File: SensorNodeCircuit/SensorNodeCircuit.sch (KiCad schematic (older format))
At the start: 12 parts

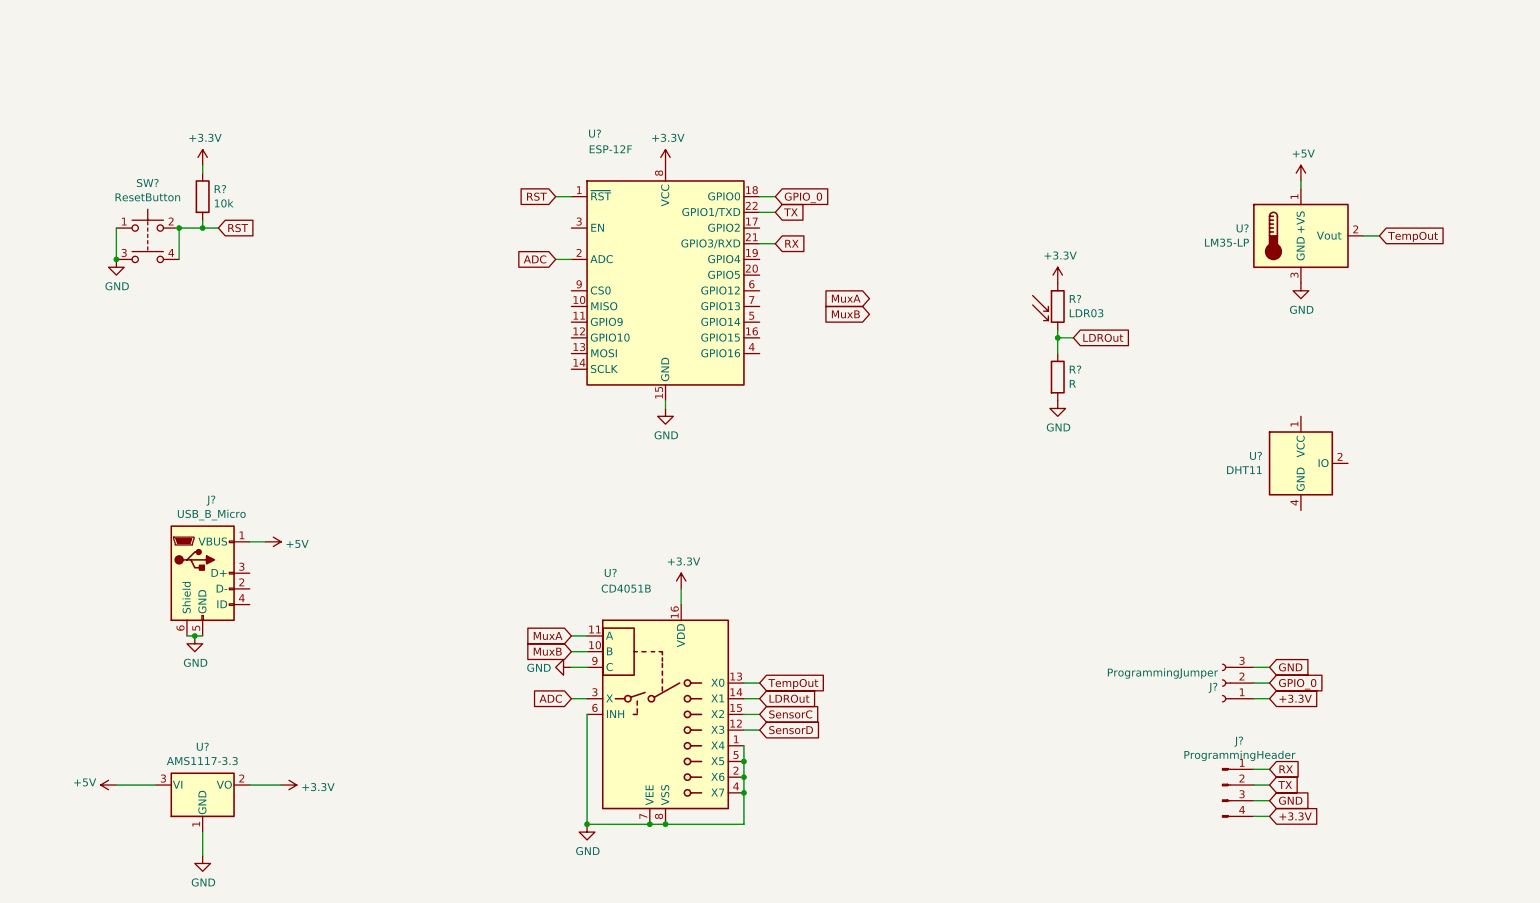
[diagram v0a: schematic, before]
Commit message: Sensor Node schematic finished
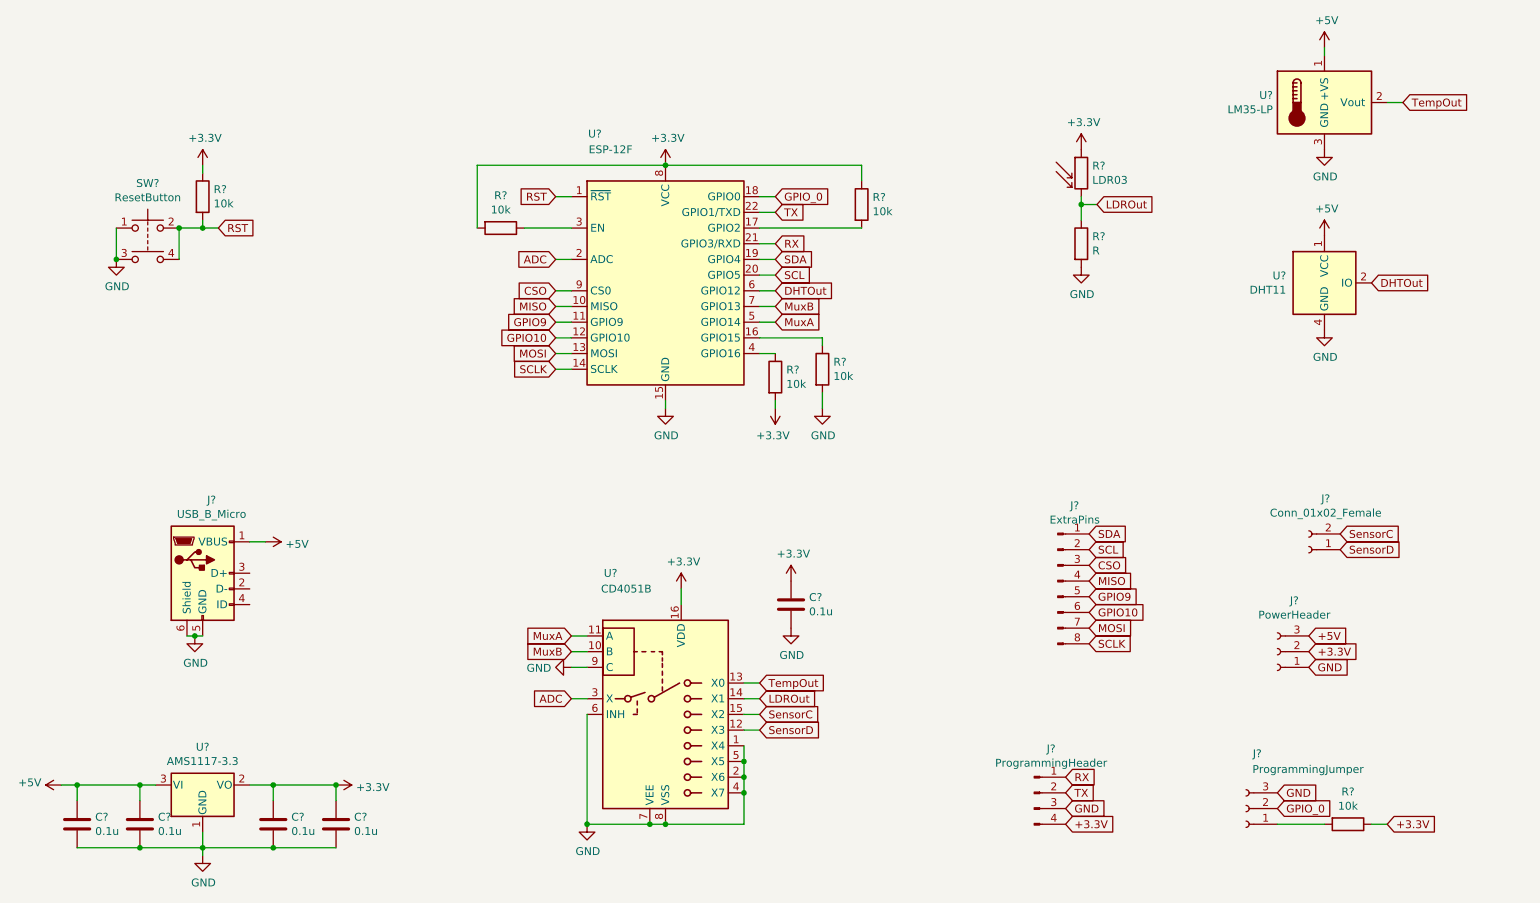
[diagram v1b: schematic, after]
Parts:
- added C? (x5): 0.1u, Capacitor_SMD:C_1206_3216Metric_Pad1.42x1.75mm_HandSolder, symbol Device:C
- added J?: ExtraPins, Connector_PinSocket_2.54mm:PinSocket_1x08_P2.54mm_Vertical, symbol Connector:Conn_01x08_Male
- added J?: PowerHeader, Connector_PinSocket_2.54mm:PinSocket_1x03_P2.54mm_Vertical, symbol Connector:Conn_01x03_Female
- added J?: Conn_01x02_Female, symbol Connector:Conn_01x02_Female
- added R? (x3): 10k, Resistor_SMD:R_1206_3216Metric_Pad1.42x1.75mm_HandSolder, symbol Device:R
- added R? (x2): 10k, Resistor_SMD:R_1206_3216Metric, symbol Device:R
- J?: footprint (none) -> Connector_USB:USB_Micro-B_Molex-105017-0001
- U?: footprint Package_DIP:DIP-16_W7.62mm_LongPads -> Package_SO:SOP-16_4.55x10.3mm_P1.27mm
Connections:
- net +3.3V: now also J?.2 (Pin_2), R?.1; no longer J?.1 (Pin_1)
- net +3V3: now also C?.1, C?.1, C?.1, R?.1, R?.2, R?.2
- net +5V: now also U?.1 (VCC), C?.1, C?.1, J?.3 (Pin_3)
- net GND: now also U?.4 (GND), C?.2, C?.2, C?.2, C?.2, C?.2, J?.1 (Pin_1), R?.2
- net MuxA: now also U?.5 (GPIO14)
- net MuxB: now also U?.7 (GPIO13)
- net SensorC: now also J?.2 (Pin_2)
- net SensorD: now also J?.1 (Pin_1)
- net MISO: now reaches U?.10 (MISO)
- net MISO: now also J?.4 (Pin_4)
- net GPIO9: now reaches U?.11 (GPIO9)
- net GPIO9: now also J?.5 (Pin_5)
- net GPIO10: now reaches U?.12 (GPIO10)
- net GPIO10: now also J?.6 (Pin_6)
- net MOSI: now reaches U?.13 (MOSI)
- net MOSI: now also J?.7 (Pin_7)
- net SCLK: now reaches U?.14 (SCLK)
- net SCLK: now also J?.8 (Pin_8)
- net at U?.16 (GPIO15): now also R?.1
- net at U?.17 (GPIO2): now also R?.2
- net SDA: now reaches U?.19 (GPIO4)
- net SDA: now also J?.1 (Pin_1)
- net SCL: now reaches U?.20 (GPIO5)
- net SCL: now also J?.2 (Pin_2)
- net at U?.3 (EN): now also R?.1
- net at U?.4 (GPIO16): now also R?.1
- net DHTOut: now reaches U?.6 (GPIO12)
- net DHTOut: now also U?.2 (IO)
- net CSO: now reaches U?.9 (CS0)
- net CSO: now also J?.3 (Pin_3)
- new net: J?.1 (Pin_1), R?.2
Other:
- moved on the sheet: J?, R?, U?

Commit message: Updated pcb footprints
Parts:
- R1: renamed from R?; footprint (none) -> Resistor_SMD:R_1206_3216Metric
- R7: renamed from R?; value R -> 220r; footprint (none) -> Resistor_SMD:R_1206_3216Metric
- U4: renamed from U?; footprint (none) -> Package_TO_SOT_THT:TO-92_Inline
- gave numbers to parts that had none: 22
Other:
- moved on the sheet: J6

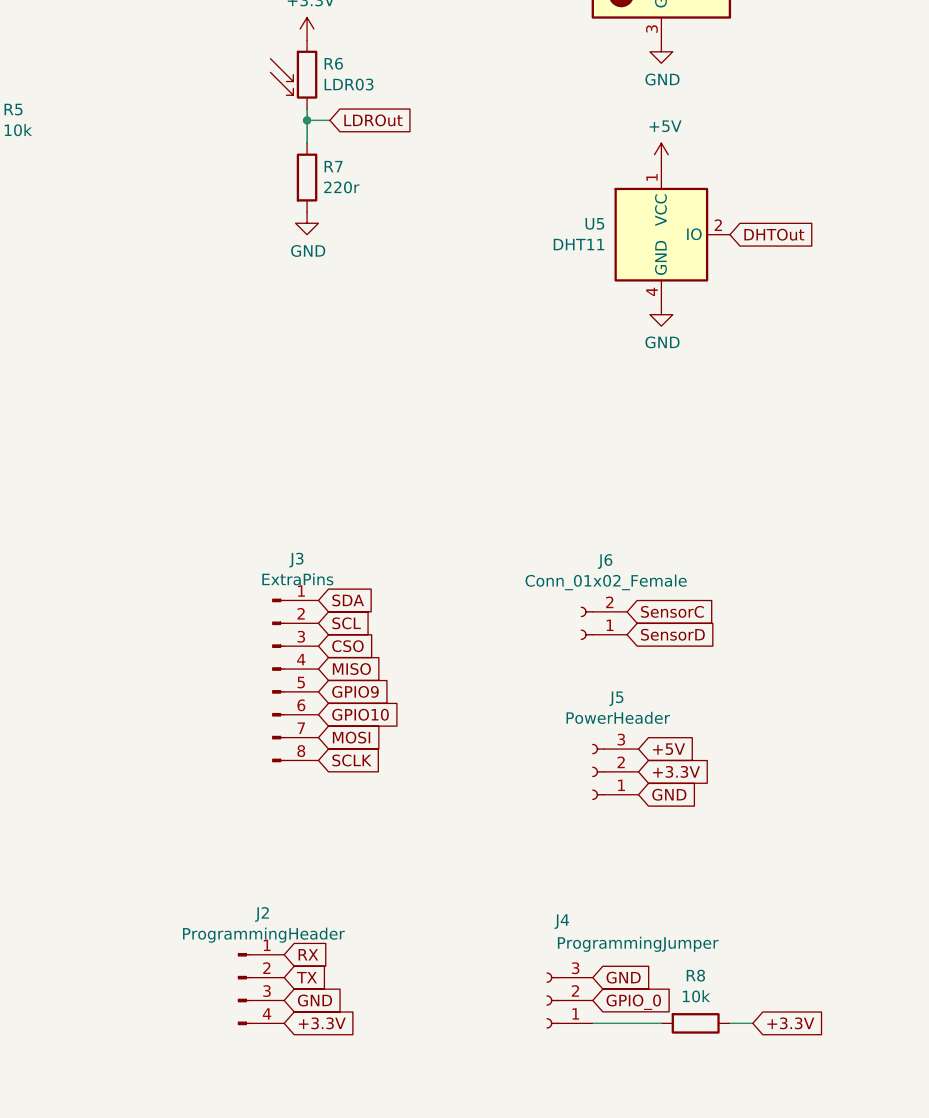
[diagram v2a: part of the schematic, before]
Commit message: Rough sensor node board layout done
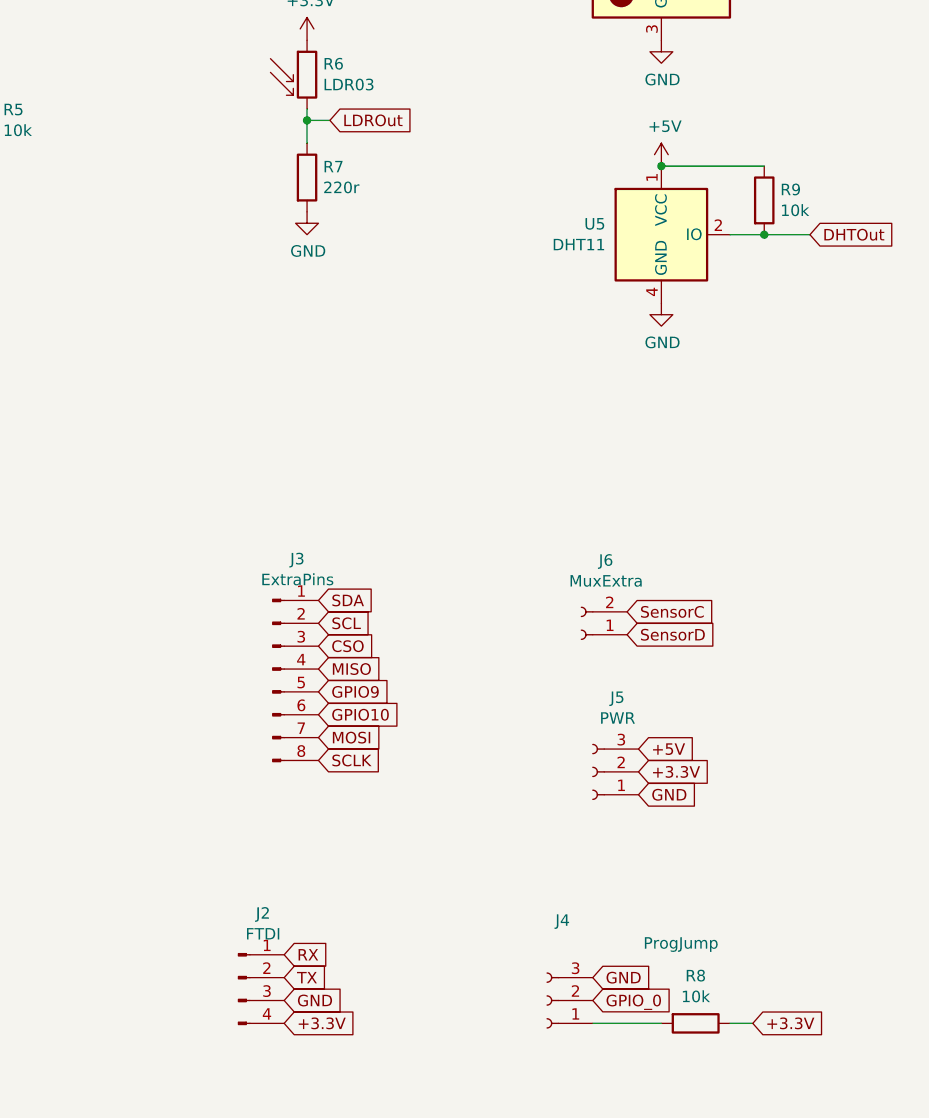
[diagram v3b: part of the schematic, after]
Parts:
- added R9: 10k, Resistor_SMD:R_1206_3216Metric_Pad1.42x1.75mm_HandSolder, symbol Device:R
- J2: value ProgrammingHeader -> FTDI
- J4: value ProgrammingJumper -> ProgJump
- J5: value PowerHeader -> PWR
- J6: value Conn_01x02_Female -> MuxExtra; footprint (none) -> Connector_PinHeader_2.54mm:PinHeader_1x02_P2.54mm_Vertical
- SW1: footprint Button_Switch_THT:SW_PUSH_6mm_H8mm -> Button_Switch_THT:SW_PUSH_6mm_H8.5mm
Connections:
- net +5V: now also R9.1
- net DHTOut: now also R9.2
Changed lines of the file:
@@
 P 7750 5750
 F 0 "J2" H 7858 6031 50  0000 C CNN
-F 1 "ProgrammingHeader" H 7858 5940 50  0000 C CNN
+F 1 "FTDI" H 7858 5940 50  0000 C CNN
 F 2 "Connector_PinHeader_2.54mm:PinHeader_1x04_P2.54mm_Vertical" H 7750 5750 50  0001 C CNN
 F 3 "~" H 7750 5750 50  0001 C CNN
@@
 P 9100 5850
 F 0 "J4" H 9000 5500 50  0000 L CNN
-F 1 "ProgrammingJumper" H 8350 5600 50  0000 L CNN
+F 1 "ProgJump" H 8350 5600 50  0000 L CNN
 F 2 "Connector_PinHeader_2.54mm:PinHeader_1x03_P2.54mm_Vertical" H 9100 5850 50  0001 C CNN
 F 3 "~" H 9100 5850 50  0001 C CNN
@@
 F 0 "SW1" H 2100 2435 50  0000 C CNN
 F 1 "ResetButton" H 2100 2344 50  0000 C CNN
-F 2 "Button_Switch_THT:SW_PUSH_6mm_H8mm" H 2100 2350 50  0001 C CNN
+F 2 "Button_Switch_THT:SW_PUSH_6mm_H8.5mm" H 2100 2350 50  0001 C CNN
 F 3 "~" H 2100 2350 50  0001 C CNN
 	1    2100 2150
@@
 	1    0    0    -1
 $EndComp
-Text GLabel 9900 2500 2    50   Input ~ 0
+Text GLabel 10250 2500 2    50   Input ~ 0
 DHTOut
 Text GLabel 6100 2550 2    50   Input ~ 0
@@
 P 9300 4850
 F 0 "J5" H 9192 4525 50  0000 C CNN
-F 1 "PowerHeader" H 9192 4616 50  0000 C CNN
+F 1 "PWR" H 9192 4616 50  0000 C CNN
 F 2 "Connector_PinSocket_2.54mm:PinSocket_1x03_P2.54mm_Vertical" H 9300 4850 50  0001 C CNN
 F 3 "~" H 9300 4850 50  0001 C CNN
@@
 P 9250 4250
 F 0 "J6" H 9142 3925 50  0000 C CNN
-F 1 "Conn_01x02_Female" H 9142 4016 50  0000 C CNN
-F 2 "" H 9250 4250 50  0001 C CNN
+F 1 "MuxExtra" H 9142 4016 50  0000 C CNN
+F 2 "Connector_PinHeader_2.54mm:PinHeader_1x02_P2.54mm_Vertical" H 9250 4250 50  0001 C CNN
 F 3 "~" H 9250 4250 50  0001 C CNN
 	1    9250 4250
@@
 Text GLabel 9450 4250 2    50   Input ~ 0
 SensorD
+$Comp
+L Device:R R9
+U 1 1 60075C43
+P 10050 2350
+F 0 "R9" H 10120 2396 50  0000 L CNN
+F 1 "10k" H 10120 2305 50  0000 L CNN
+F 2 "Resistor_SMD:R_1206_3216Metric_Pad1.42x1.75mm_HandSolder" V 9980 2350 50  0001 C CNN
+F 3 "~" H 10050 2350 50  0001 C CNN
+	1    10050 2350
+	1    0    0    -1
+$EndComp
+Wire Wire Line
+	10250 2500 10050 2500
+Connection ~ 10050 2500
+Wire Wire Line
+	10050 2500 9900 2500
+Wire Wire Line
+	10050 2200 9600 2200
+Connection ~ 9600 2200
 $EndSCHEMATC

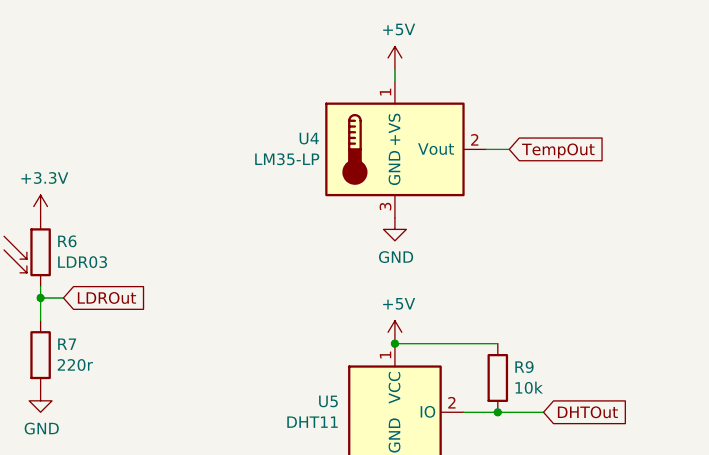
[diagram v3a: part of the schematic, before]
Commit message: Sensor node pcb updated
Added voltage divider to temp sensor output, and thicker power traces
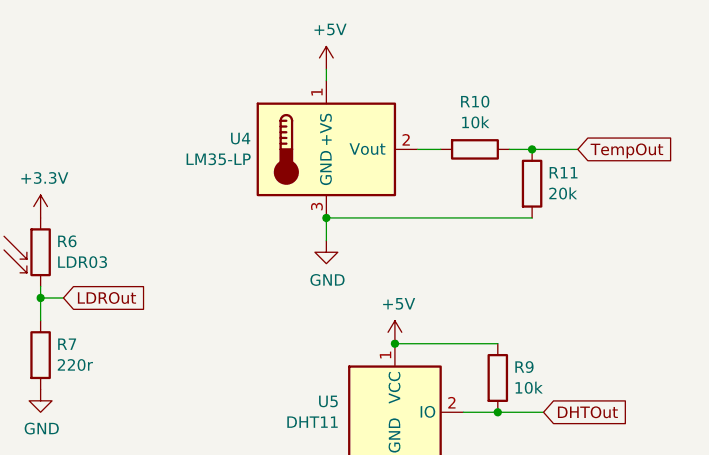
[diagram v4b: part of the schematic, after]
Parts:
- added R10: 10k, Resistor_SMD:R_1206_3216Metric, symbol Device:R
- added R11: 20k, Resistor_SMD:R_1206_3216Metric, symbol Device:R
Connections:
- net GND: now also R11.2
- net TempOut: now also R10.1, R11.1; no longer U4.2 (Vout)
- new net: R10.2, U4.2 (Vout)
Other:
- moved on the sheet: U4
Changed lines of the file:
@@
 L Sensor_Temperature:LM35-LP U4
 U 1 1 5FE06B79
-P 9600 1350
-F 0 "U4" H 9271 1396 50  0000 R CNN
-F 1 "LM35-LP" H 9271 1305 50  0000 R CNN
-F 2 "Package_TO_SOT_THT:TO-92_Inline" H 9650 1100 50  0001 L CNN
-F 3 "http://www.ti.com/lit/ds/symlink/lm35.pdf" H 9600 1350 50  0001 C CNN
-	1    9600 1350
+P 9300 1350
+F 0 "U4" H 8971 1396 50  0000 R CNN
+F 1 "LM35-LP" H 8971 1305 50  0000 R CNN
+F 2 "Package_TO_SOT_THT:TO-92_Inline" H 9350 1100 50  0001 L CNN
+F 3 "http://www.ti.com/lit/ds/symlink/lm35.pdf" H 9300 1350 50  0001 C CNN
+	1    9300 1350
 	1    0    0    -1
 $EndComp
@@
 Wire Wire Line
 	6000 5150 5900 5150
-Text GLabel 10100 1350 2    50   Input ~ 0
+Text GLabel 10400 1350 2    50   Input ~ 0
 TempOut
 Wire Wire Line
-	10100 1350 10000 1350
+	9800 1350 9700 1350
 $Comp
 L power:GND #PWR0102
@@
 L power:GND #PWR0106
 U 1 1 5FE428FB
-P 9600 1650
-F 0 "#PWR0106" H 9600 1400 50  0001 C CNN
-F 1 "GND" H 9605 1477 50  0000 C CNN
-F 2 "" H 9600 1650 50  0001 C CNN
-F 3 "" H 9600 1650 50  0001 C CNN
-	1    9600 1650
+P 9300 1750
+F 0 "#PWR0106" H 9300 1500 50  0001 C CNN
+F 1 "GND" H 9305 1577 50  0000 C CNN
+F 2 "" H 9300 1750 50  0001 C CNN
+F 3 "" H 9300 1750 50  0001 C CNN
+	1    9300 1750
 	1    0    0    -1
 $EndComp
@@
 L power:+5V #PWR0115
 U 1 1 5FE7F6C6
-P 9600 1000
-F 0 "#PWR0115" H 9600 850 50  0001 C CNN
-F 1 "+5V" H 9615 1173 50  0000 C CNN
-F 2 "" H 9600 1000 50  0001 C CNN
-F 3 "" H 9600 1000 50  0001 C CNN
-	1    9600 1000
-	1    0    0    -1
-$EndComp
-Wire Wire Line
-	9600 1000 9600 1050
+P 9300 1000
+F 0 "#PWR0115" H 9300 850 50  0001 C CNN
+F 1 "+5V" H 9315 1173 50  0000 C CNN
+F 2 "" H 9300 1000 50  0001 C CNN
+F 3 "" H 9300 1000 50  0001 C CNN
+	1    9300 1000
+	1    0    0    -1
+$EndComp
+Wire Wire Line
+	9300 1000 9300 1050
 $Comp
 L Device:R R1
@@
 	10050 2200 9600 2200
 Connection ~ 9600 2200
+$Comp
+L Device:R R10
+U 1 1 600279B7
+P 9950 1350
+F 0 "R10" V 9743 1350 50  0000 C CNN
+F 1 "10k" V 9834 1350 50  0000 C CNN
+F 2 "Resistor_SMD:R_1206_3216Metric" V 9880 1350 50  0001 C CNN
+F 3 "~" H 9950 1350 50  0001 C CNN
+	1    9950 1350
+	0    1    1    0
+$EndComp
+$Comp
+L Device:R R11
+U 1 1 6002DC68
+P 10200 1500
+F 0 "R11" H 10270 1546 50  0000 L CNN
+F 1 "20k" H 10270 1455 50  0000 L CNN
+F 2 "Resistor_SMD:R_1206_3216Metric" V 10130 1500 50  0001 C CNN
+F 3 "~" H 10200 1500 50  0001 C CNN
+	1    10200 1500
+	1    0    0    -1
+$EndComp
+Wire Wire Line
+	10100 1350 10200 1350
+Connection ~ 10200 1350
+Wire Wire Line
+	10200 1350 10400 1350
+Wire Wire Line
+	10200 1650 9300 1650
+Wire Wire Line
+	9300 1750 9300 1650
+Connection ~ 9300 1650
 $EndSCHEMATC
